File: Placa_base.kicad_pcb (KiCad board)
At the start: 2 copper layers, 221 parts, among them J1 JTAG/SWD, J10 Interfaz con entradas digital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, J11 I2C1, J12 I2C3, J13 CAN1, J14 SPI1, J15 Conn_02x08_Odd_Even, J2 Bateria, J3 Entrada 24V, J4 RS-485, J5 TV_6V, J6 AN1, J7 AN2, J8 Micro_SD_Card_Det_Hirose_DM3AT, J9 Salidas 5V, Q1 MMBT3904, Q2 MMBT3904, Q3 MMBT3904, Q4 AO3401, Q5 AO3401, Q6 MMBT3904, Q7 MMBT3904, Q8 MMBT3904, Q9 MMBT3904, SW1 SW_Push, SW2 SW_Push, SW3 SW_Push, U1 STM32F407VGTx, U10 MCP6L04T-E/ST, U11 74HCT541, U2 DC-DC_Step-Down, U3 AZ1117-3.3, U4 AZ1117-3.3, U5 RFM-0505S, U6 ISO1412, U7 NodeMCU_1.0_(ESP-12E), U8 SIM800L_modulo, U9 Modulo_A6_Mini, Y1 32.768KHz, Y2 8MHz

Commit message: v0.16
Correcciones en PCB.
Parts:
- added R7: 0, Resistor_SMD:R_0603_1608Metric_Pad1.05x0.95mm_HandSolder, F.Cu at (203.8, 72.0)
- H1, H2, H3, H4: value MountingHole -> MountingHole_Pad; footprint MountingHole:MountingHole_3mm -> MountingHole:MountingHole_3.5mm_Pad
- J1: value JTAG/SWD -> SWD/STLINK; footprint Connector_IDC:IDC-Header_2x05_P2.54mm_Vertical -> Connector_PinHeader_2.54mm:PinHeader_1x06_P2.54mm_Vertical
- moved C34 48.2 mm to (247.4, 91.2)
- moved C5 33.8 mm to (143.0, 74.9), turned to 90 degrees
- moved C8 28.8 mm to (147.3, 82.8), turned to 0 degrees
- moved R17 18.6 mm to (99.6, 44.7), turned to 180 degrees
- moved U9 16.2 mm to (162.5, 132.8), turned to 90 degrees
- moved FB1 13.4 mm to (218.9, 79.8)
- moved C30 12.9 mm to (213.4, 77.9), turned to 180 degrees
- moved C29 9.88 mm to (213.4, 75.3), turned to 180 degrees
- moved C10 8.67 mm to (127.5, 75.7)
- moved J1 8.10 mm to (98.8, 118.1)
- moved C58 7.85 mm to (226.1, 49.3)
- moved R57 7.85 mm to (224.3, 49.3)
- moved U4 7.46 mm to (221.8, 72.8), turned to 0 degrees
- moved C33 7.21 mm to (213.3, 72.6), turned to 180 degrees
- moved C31 7.03 mm to (213.4, 67.1), turned to 180 degrees
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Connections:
- C13 pad 2: GND -> GNDA
- C14 pad 2: GND -> GNDA
- C15 pad 2: GND -> GNDA
- C16 pad 2: GND -> GNDA
- C17 pad 2: GND -> GNDA
- C18 pad 2: GND -> GNDA
- C29 pad 2: GND -> GNDA
- C30 pad 2: GND -> GNDA
- C31 pad 2: GND -> GNDA
- C32 pad 2: GND -> GNDA
- C33 pad 2: GND -> GNDA
- C46 pad 2: GND -> GNDA
- C47 pad 2: GND -> GNDA
- C48 pad 2: GND -> GNDA
- C49 pad 2: GND -> GNDA
- C50 pad 2: GND -> GNDA
- C51 pad 2: GND -> GNDA
- C52 pad 2: GND -> GNDA
- C54 pad 2: GND -> GNDA
- C55 pad 2: GND -> GNDA
- C57 pad 2: GND -> GNDA
- C58 pad 2: GND -> GNDA
- D13 pad 1: GND -> GNDA
- D14 pad 2: GND -> GNDA
- D16 pad 2: GND -> GNDA
- D18 pad 1: GND -> GNDA
- D19 pad 1: GND -> GNDA
- D20 pad 1: GND -> GNDA
- H1 pad 1: (no net) -> Net-(H1-Pad1)
- H2 pad 1: (no net) -> Net-(H1-Pad1)
- H3 pad 1: (no net) -> Net-(H1-Pad1)
- H4 pad 1: (no net) -> Net-(H1-Pad1)
- J1 pad 2: /MCU/TMS-SWDIO -> /MCU/TCK-SWCLK
- J1 pad 4: /MCU/TCK-SWCLK -> /MCU/TMS-SWDIO
- J1 pad 5: GND -> /NRST
- J6 pad 1: GND -> GNDA
- J7 pad 1: GND -> GNDA
- R41 pad 2: GND -> GNDA
- R42 pad 2: GND -> GNDA
- R45 pad 2: GND -> GNDA
- R46 pad 2: GND -> GNDA
- R49 pad 2: GND -> GNDA
- R51 pad 1: GND -> GNDA
- R52 pad 2: GND -> GNDA
- R53 pad 1: GND -> GNDA
- R56 pad 2: GND -> GNDA
- R58 pad 1: GND -> GNDA
- R59 pad 2: GND -> GNDA
- R60 pad 1: GND -> GNDA
- U1 pad 20: GND -> GNDA
- U10 pad 11: GND -> GNDA
- U4 pad 1: GND -> GNDA
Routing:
- net Net-(H1-Pad1): track 0.00 -> 1126.9 mm, vias 0 -> 112
- net GND: track 477.8 -> 263.9 mm, vias 87 -> 58
- net GNDA: track 0.00 -> 143.1 mm, vias 0 -> 30
- net /MCU/TDI: track 62.0 -> 0.00 mm
- net /PD6: track 86.9 -> 49.5 mm
- net /PD5: track 84.2 -> 48.3 mm
- net /PD3: track 54.8 -> 77.5 mm
- net Net-(D12-Pad2): track 16.3 -> 38.5 mm
- net +5V: track 527.6 -> 505.7 mm
- net Net-(R33-Pad2): track 8.32 -> 29.1 mm
- net Net-(J4-Pad5): track 7.28 -> 27.8 mm
- net VDDA: track 211.6 -> 191.5 mm, vias 11 -> 12
- net Net-(C45-Pad1): track 11.0 -> 26.8 mm
- net /PC11: track 43.7 -> 28.5 mm
- net /PA3: track 72.0 -> 57.9 mm, vias 0 -> 2
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- added copper zone on B.Cu, net GNDA
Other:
- board text added: "0-10V"
- board text added: "0-20mA"
- board text added: "1-2"
- board text added: "2-3"
- board text added: "3V3"
- board text added: "3V3-3V3 GND-GND NC -PC4 PE13-PC5 PE12-PB0 PE11-PB1 PE10-PE7 PE9-PE8"
- board text added: "3V3-GND MOSI-NSS MISO-CLK"
- board text added: "3V3-GND SCL-SCA"
- board text added: "A"
- board text added: "B"
- board text added: "BOOT0"
- board text added: "BOOT1"
- board text added: "CLK"
- board text added: "DIO"
- board text added: "Entradas Analogicas"
- board text added: "GND"
- board text added: "GND S-IN S-Out P/S CLK 5V"
- board text added: "JP5/7"
- board text added: "JP6/8"
- board text added: "NO"
- board text added: "PB12"
- board text added: "PB13"
- board text added: "PB14"
- board text added: "PB15"
- board text added: "RS-485"
- board text added: "RST"
- board text added: "SDA-3V3 SCL-GND"
- board text added: "SI"
- board text added: "SWD"
- board text added: "SWO"
- board text added: "TX-3V3 RX-GND"
- board text added: "Y"
- board text added: "Z"
- board text removed: "ABZY-"
- board text removed: "GND GND S-Out P/S CLK"
- board text removed: "JTAG/SWD"

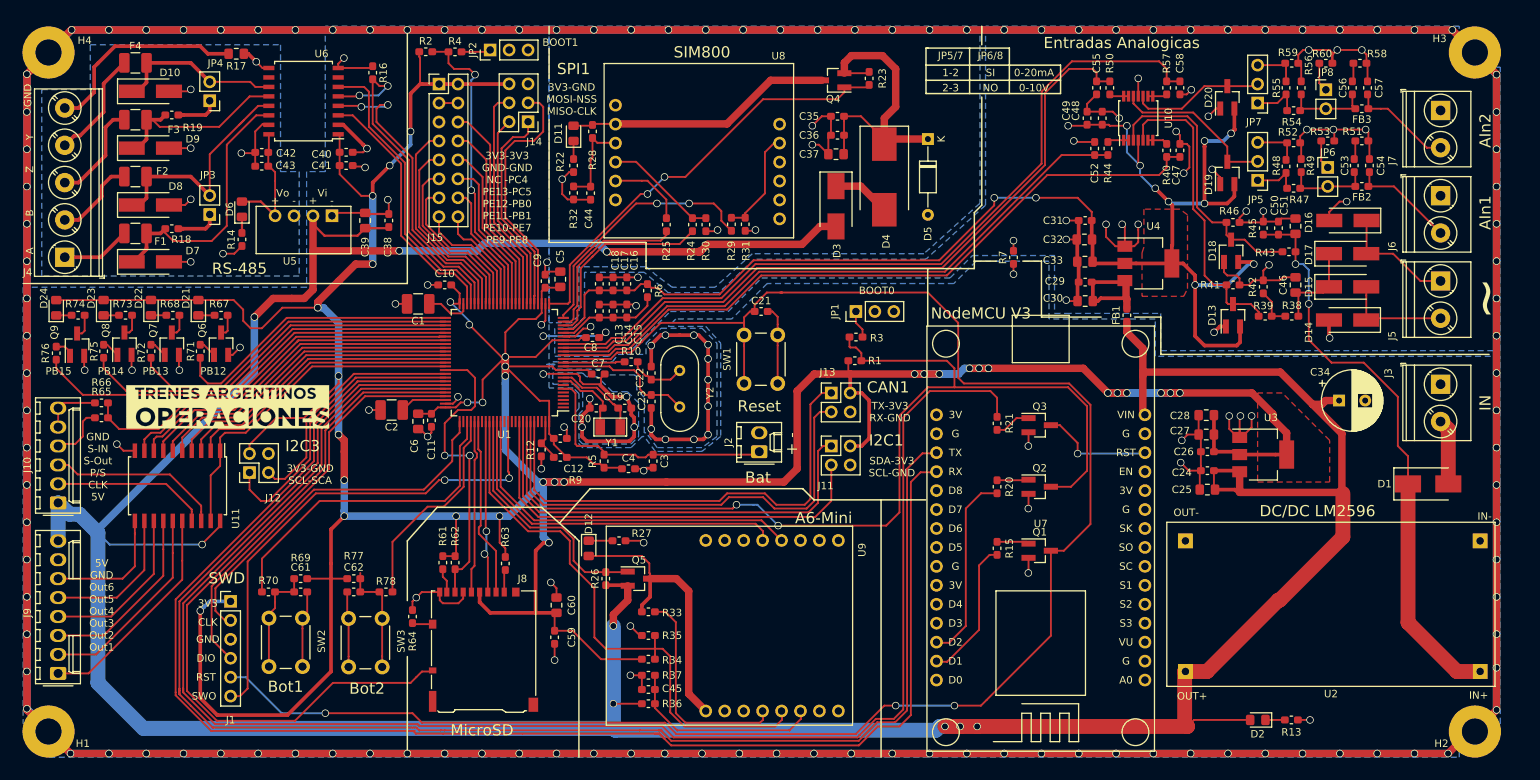
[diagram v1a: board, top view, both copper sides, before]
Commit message: Modificaciones en planos de masa
Se cambiaron algunas pistas y se agregó plano superior junto a vías para mejorar la impedancia.
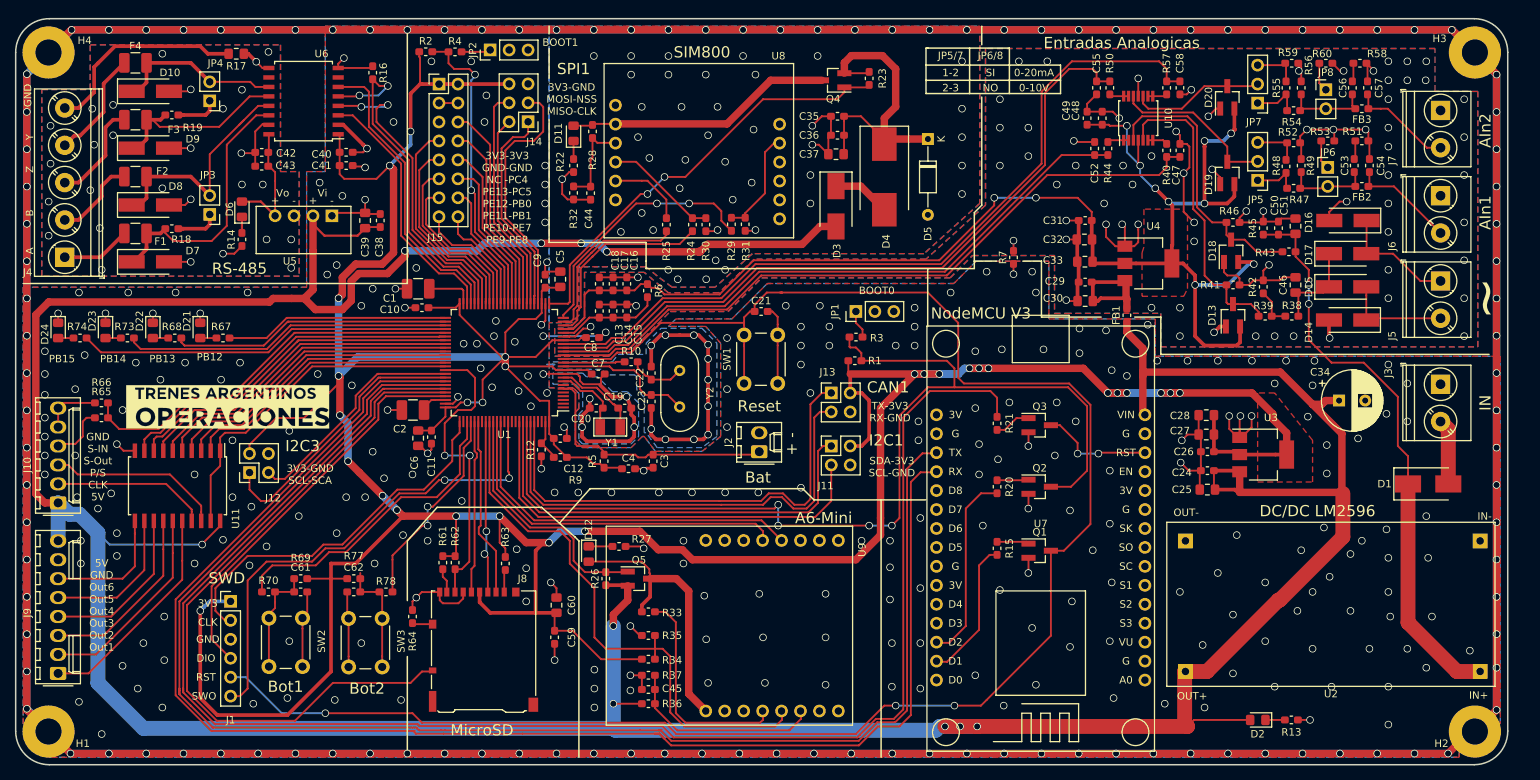
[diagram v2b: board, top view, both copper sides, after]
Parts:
- removed Q6, Q7, Q8, Q9: MMBT3904, Package_TO_SOT_SMD:SOT-23_Handsoldering
- removed R71, R72, R75, R76: 5K6, Resistor_SMD:R_0603_1608Metric_Pad1.05x0.95mm_HandSolder
- R61, R62, R63: value 5K6 -> 56K
- moved C10 4.31 mm to (124.5, 78.7)
- moved D22 3.07 mm to (88.4, 81.8), turned to 270 degrees
- moved D21 3.06 mm to (94.7, 81.8), turned to 270 degrees
- moved D23 3.06 mm to (82.0, 81.8), turned to 270 degrees
- moved R67 3.06 mm to (97.8, 82.8)
- moved R68 3.06 mm to (91.3, 82.8)
- moved R73 3.06 mm to (85.0, 82.8)
- moved R74 3.06 mm to (78.6, 82.8)
- moved D24 3.05 mm to (75.7, 81.8), turned to 270 degrees
- moved C2 2.85 mm to (123.2, 92.5)
- moved C11 2.25 mm to (125.7, 96.1)
- moved C6 2.25 mm to (124.0, 96.2)
- moved C1 2.03 mm to (124.0, 76.2)
- moved C38 1.14 mm to (118.9, 67.1)
- moved D12 0.76 mm to (146.8, 111.8)
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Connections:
- D21 pad 1: Net-(D21-Pad1) -> GND
- D21 pad 2: VDD -> Net-(D21-Pad2)
- D22 pad 1: Net-(D22-Pad1) -> GND
- D22 pad 2: VDD -> Net-(D22-Pad2)
- D23 pad 1: Net-(D23-Pad1) -> GND
- D23 pad 2: VDD -> Net-(D23-Pad2)
- D24 pad 1: Net-(D24-Pad1) -> GND
- D24 pad 2: VDD -> Net-(D24-Pad2)
- H1 pad 1: Net-(H1-Pad1) -> GND
- H2 pad 1: Net-(H1-Pad1) -> GND
- H3 pad 1: Net-(H1-Pad1) -> GND
- H4 pad 1: Net-(H1-Pad1) -> GND
- R67 pad 1: Net-(Q6-Pad3) -> /PB12
- R67 pad 2: Net-(D21-Pad1) -> Net-(D21-Pad2)
- R68 pad 1: Net-(Q7-Pad3) -> /PB13
- R68 pad 2: Net-(D22-Pad1) -> Net-(D22-Pad2)
- R73 pad 1: Net-(Q8-Pad3) -> /PB14
- R73 pad 2: Net-(D23-Pad1) -> Net-(D23-Pad2)
- R74 pad 1: Net-(Q9-Pad3) -> /PB15
- R74 pad 2: Net-(D24-Pad1) -> Net-(D24-Pad2)
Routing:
- net Net-(H1-Pad1): track 1126.9 -> 0.00 mm, vias 112 -> 0
- net GND: track 263.9 -> 1390.3 mm, vias 58 -> 435
- net VDD: track 600.8 -> 574.1 mm, vias 35 -> 29
- net +5V: track 505.7 -> 531.1 mm, vias 9 -> 10
- net /PB12: track 39.4 -> 30.1 mm
- net /PB15: track 58.5 -> 50.2 mm
- net /PB14: track 52.1 -> 44.0 mm
- net /PB13: track 45.4 -> 37.5 mm
- net GNDA: track 143.1 -> 139.8 mm, vias 30 -> 72
- net Net-(Q9-Pad3): track 3.24 -> 0.00 mm
- net Net-(Q8-Pad3): track 3.11 -> 0.00 mm
- net Net-(Q7-Pad3): track 3.11 -> 0.00 mm
- net Net-(Q6-Pad3): track 3.06 -> 0.00 mm
- net Net-(Q9-Pad1): track 2.68 -> 0.00 mm
- net Net-(C2-Pad1): track 6.28 -> 3.78 mm
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- added copper zone on F.Cu, net Earth
- added copper zone on F.Cu, net GND
- added copper zone on F.Cu, net GNDA
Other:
- board outline added: 200 x 100 mm

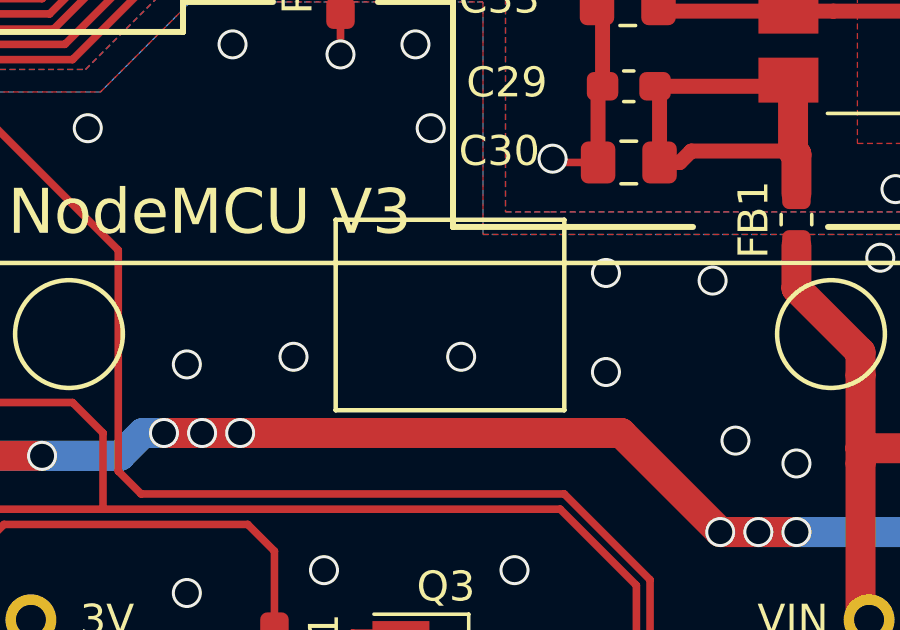
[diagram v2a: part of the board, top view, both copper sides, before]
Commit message: v0.19 pasa ERC con 0 errores/warnings.
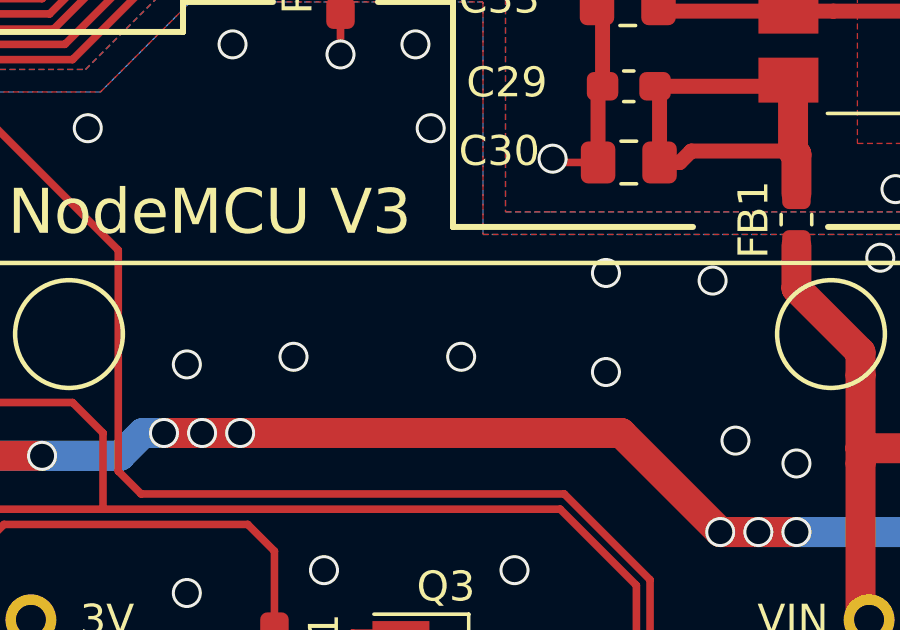
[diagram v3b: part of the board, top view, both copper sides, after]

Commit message: Modificaciones en PCB
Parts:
- moved H2 0.11 mm to (265.5, 135.5)
- moved H1 0.11 mm to (74.5, 135.5)
- moved H3 0.10 mm to (265.5, 44.5)
- moved H4 0.10 mm to (74.5, 44.5)
- turned R13 to 0 degrees
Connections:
- J15 pad 5: Net-(J15-Pad5) -> (no net)
- J3 pad 1: GND -> Net-(J3-Pad1)
- JP1 pad 3: Net-(JP1-Pad3) -> (no net)
- JP2 pad 3: Net-(JP2-Pad3) -> (no net)
- R13 pad 1: GND -> Net-(D2-Pad1)
- R13 pad 2: Net-(D2-Pad1) -> GND
- U1 pad 1: /MCU/PE2 -> (no net)
- U1 pad 2: /MCU/PE3 -> (no net)
- U1 pad 3: /MCU/PE4 -> (no net)
- U1 pad 4: /MCU/PE5 -> (no net)
- U1 pad 5: /MCU/PE6 -> (no net)
- U1 pad 7: /MCU/PC13 -> (no net)
- U1 pad 77: /MCU/TDI -> (no net)
- U1 pad 82: /MCU/PD1 -> (no net)
- U1 pad 88: /MCU/PD7 -> (no net)
- U1 pad 90: /MCU/NTRST -> (no net)
- U1 pad 91: /MCU/PB5 -> (no net)
- U1 pad 97: /MCU/PE0 -> (no net)
- U1 pad 98: /MCU/PE1 -> (no net)
- U2 pad 2: GND -> Net-(J3-Pad1)
- U6 pad 10: Net-(U6-Pad10) -> (no net)
- U6 pad 7: Net-(U6-Pad7) -> (no net)
- U7 pad 1: Net-(U7-Pad1) -> (no net)
- U7 pad 11: Net-(U7-Pad11) -> (no net)
- U7 pad 12: Net-(U7-Pad12) -> (no net)
- U7 pad 16: Net-(U7-Pad16) -> (no net)
- U7 pad 2: Net-(U7-Pad2) -> (no net)
- U7 pad 20: Net-(U7-Pad20) -> (no net)
- U7 pad 21: Net-(U7-Pad21) -> (no net)
- U7 pad 22: Net-(U7-Pad22) -> (no net)
- U7 pad 23: Net-(U7-Pad23) -> (no net)
- U7 pad 25: Net-(U7-Pad25) -> (no net)
- U7 pad 26: Net-(U7-Pad26) -> (no net)
- U7 pad 27: Net-(U7-Pad27) -> (no net)
- U7 pad 3: Net-(U7-Pad3) -> (no net)
- U7 pad 30: Net-(U7-Pad30) -> (no net)
- U7 pad 4: Net-(U7-Pad4) -> (no net)
- U7 pad 5: Net-(U7-Pad5) -> (no net)
- U7 pad 6: Net-(U7-Pad6) -> (no net)
- U7 pad 7: Net-(U7-Pad7) -> (no net)
- U7 pad 8: Net-(U7-Pad8) -> (no net)
- U7 pad 9: Net-(U7-Pad9) -> (no net)
- U8 pad 1: Net-(U8-Pad1) -> (no net)
- U8 pad 10: Net-(U8-Pad10) -> (no net)
- U8 pad 12: Net-(U8-Pad12) -> (no net)
- U8 pad 7: Net-(U8-Pad7) -> (no net)
- U8 pad 8: Net-(U8-Pad8) -> (no net)
- U8 pad 9: Net-(U8-Pad9) -> (no net)
- U9 pad 10: Net-(U9-Pad10) -> (no net)
- U9 pad 11: Net-(U9-Pad11) -> (no net)
- U9 pad 15: Net-(U9-Pad15) -> (no net)
- U9 pad 16: Net-(U9-Pad16) -> (no net)
- U9 pad 2: Net-(U9-Pad2) -> (no net)
- U9 pad 3: Net-(U9-Pad3) -> (no net)
- U9 pad 7: Net-(U9-Pad7) -> (no net)
- U9 pad 8: Net-(U9-Pad8) -> (no net)
- U9 pad 9: Net-(U9-Pad9) -> (no net)
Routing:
- net GNDA: track 139.8 -> 101.3 mm, vias 72 -> 76
- net Net-(J3-Pad1): track 0.00 -> 24.5 mm
- net GND: track 1390.3 -> 1396.5 mm, vias 435 -> 434
- net +5V: track 531.1 -> 529.8 mm

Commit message: Importantes mejoras en PCB
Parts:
- removed H5: Logo_TA, Propios:ta2
- added G1: TrenesArgentinosLogo, Propios:TrenesArgentinosLogoNeg, F.Cu at (98.7, 91.8)
- moved R61 18.1 mm to (142.8, 122.2), turned to 0 degrees
- moved R62 15.8 mm to (142.8, 120.5), turned to 0 degrees
- moved SW1 13.4 mm to (175.5, 78.0), turned to 270 degrees
- moved C59 12.9 mm to (132.5, 114.5), turned to 0 degrees
- moved C60 12.8 mm to (131.8, 111.8)
- moved C21 9.46 mm to (178.2, 83.8), turned to 90 degrees
- moved C38 7.52 mm to (112.0, 64.0), turned to 0 degrees
- moved C34 7.31 mm to (247.5, 98.5)
- moved C39 6.83 mm to (112.2, 62.0), turned to 0 degrees
- moved C31 6.41 mm to (215.0, 73.2)
- moved D2 4.75 mm to (231.8, 134.0)
- moved R13 4.75 mm to (236.2, 134.0)
- moved C1 4.52 mm to (127.8, 73.8)
- moved R34 4.11 mm to (154.8, 121.8)
- moved R12 4.09 mm to (141.5, 101.8), turned to 180 degrees
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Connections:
- net /PB12 renamed /LED1
- net /PB13 renamed /LED2
- net /PB14 renamed /LED3
- net /PB15 renamed /LED4
- net /PC0 renamed /An_In1
- net /PC1 renamed /An_In2
- net /PC10 renamed /SW1
- net /PC11 renamed /SW2
- net /PC2 renamed /An_In3
- net /PC3 renamed /An_In4
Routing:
- net GND: track 1396.5 -> 1344.0 mm, vias 434 -> 425
- net +5V: track 529.8 -> 581.8 mm, vias 10 -> 5
- net VDD: track 574.1 -> 524.2 mm, vias 29 -> 4
- net /BOOT0: track 139.5 -> 123.1 mm, vias 4 -> 0
- net Net-(J8-Pad8): track 3.29 -> 17.1 mm
- net /PA11: track 217.3 -> 203.8 mm
- net /PD2: track 23.0 -> 31.6 mm, vias 2 -> 0
- net GNDA: track 101.3 -> 93.1 mm, vias 76 -> 78
- net /PC8: track 40.6 -> 48.1 mm
- net /PA9: track 202.1 -> 194.6 mm
- net /PB8: track 63.4 -> 56.3 mm
- net /PA10: track 201.1 -> 194.5 mm
- net Net-(C29-Pad1): track 15.6 -> 9.29 mm
- net /SW1: track 41.8 -> 35.5 mm
- net /PB9: track 64.3 -> 58.1 mm
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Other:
- board text added: "5V"
- board text added: "CONICET-GICSAFe"
